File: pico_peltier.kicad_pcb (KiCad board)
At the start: 4 copper layers, 56 x 88 mm, 99 parts, among them J1 USB_C_Receptacle_USB2.0_14P, J2 Conn_02x07_Odd_Even, J3 ZJY130-2864KSWLG22, J4 Screw_Terminal_01x02, SW1 SW_Push, SW2 SW_Push, SW3 RotaryEncoder_Switch, U1 W25Q128JVS, U2 RP2350_60QFN, U3 WE-TVS-82400102, U4 LT8722AV-PBF, U5 TPSM863253RDXR, Y1 ABM8-272-T3

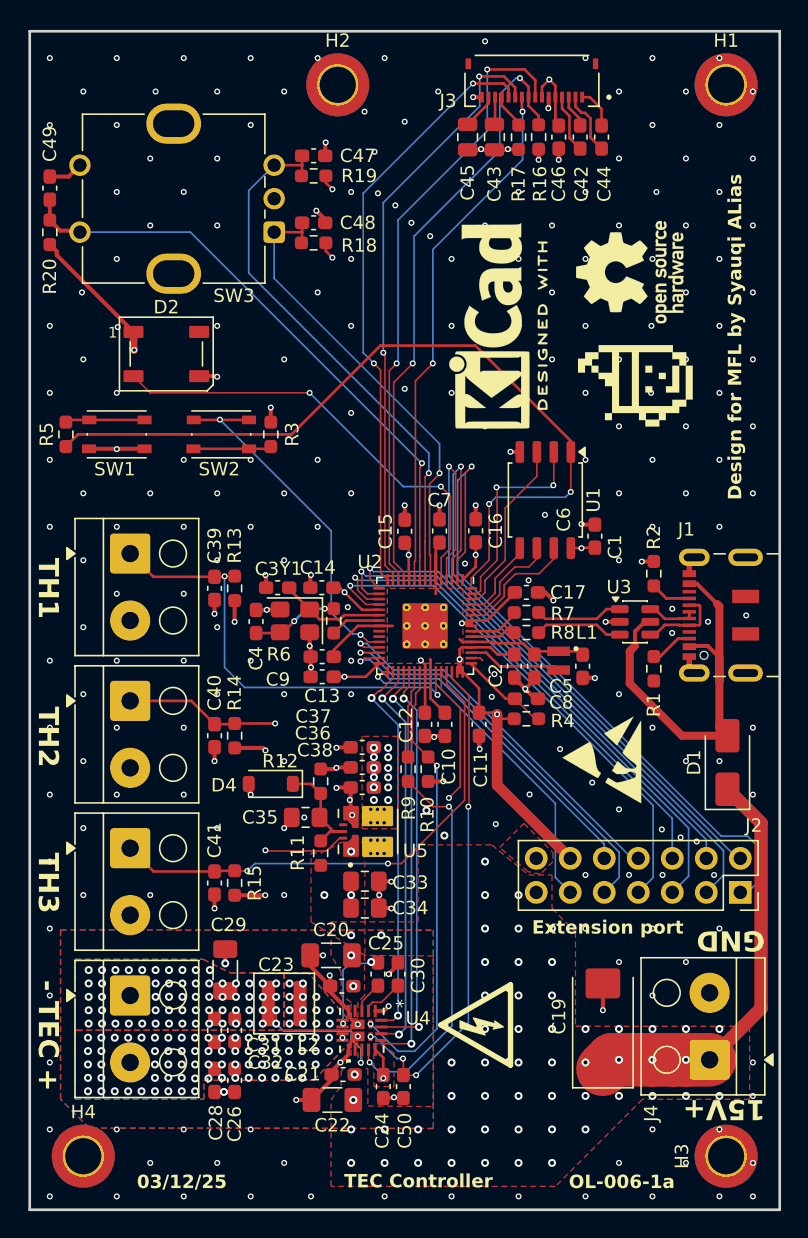
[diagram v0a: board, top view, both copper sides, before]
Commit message: fix silkscreen
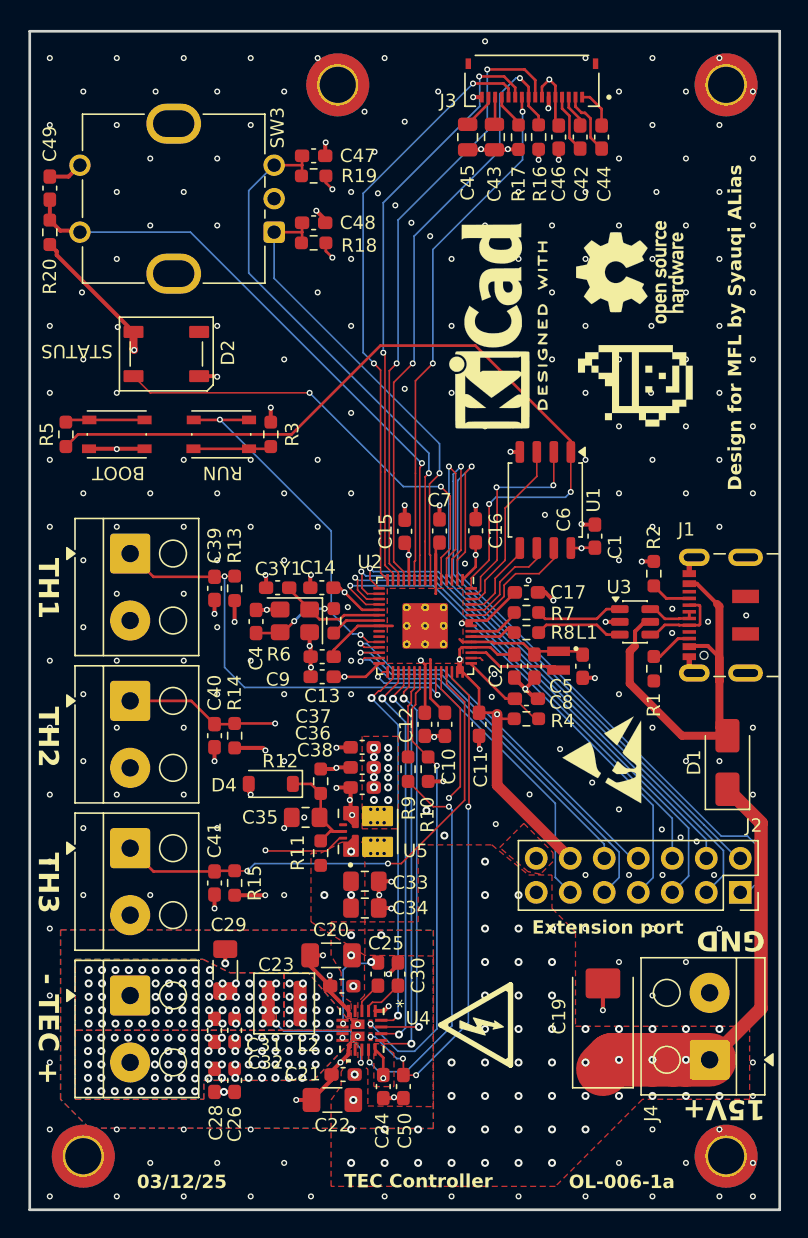
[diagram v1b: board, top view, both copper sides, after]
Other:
- board text added: "BOOT"
- board text added: "RUN"
- board text added: "STATUS"
